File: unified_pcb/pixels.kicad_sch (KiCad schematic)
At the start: 291 parts

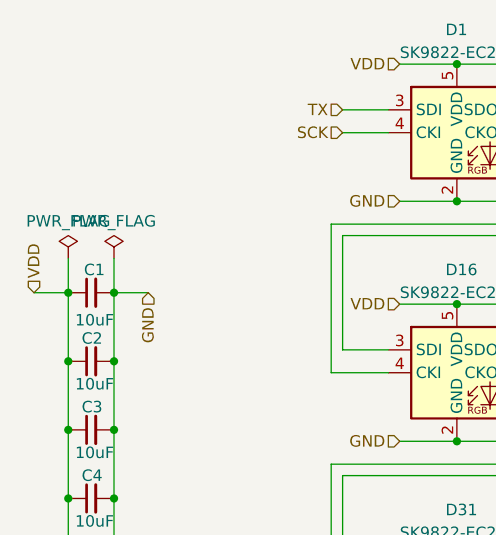
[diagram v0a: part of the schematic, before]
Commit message: change BQ27421 back to BQ27427
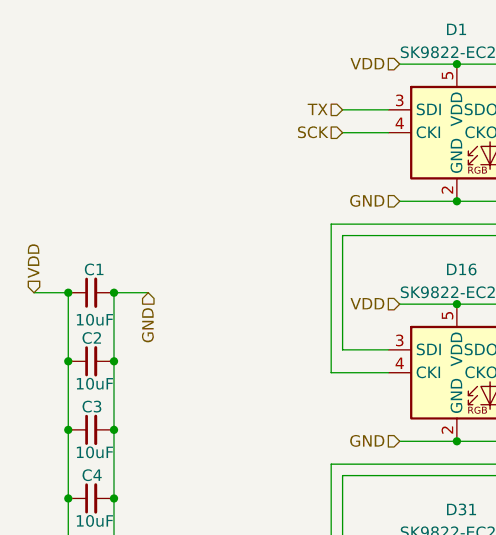
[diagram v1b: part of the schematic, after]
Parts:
- D1, D10, D100, D101, D102, D103, D104, D105, D106, D107, D108, D109, D11, D110, D111, D112, D113, D114, D115, D116, D117, D118, D119, D12, D120, D121, D122, D123, D124, D125, D126, D127, D128, D129, D13, D130, D131, D132, D133, D134, D135, D136, D137, D138, D139, D14, D140, D141, D142, D143, D144, D145, D146, D147, D148, D149, D15, D150, D151, D152, D153, D154, D155, D156, D157, D158, D159, D16, D160, D161, D162, D163, D164, D165, D166, D167, D168, D169, D17, D170, D171, D172, D173, D174, D175, D176, D177, D178, D179, D18, D180, D181, D182, D183, D184, D185, D186, D187, D188, D189, D19, D190, D191, D192, D193, D194, D195, D196, D197, D198, D199, D2, D20, D200, D201, D202, D203, D204, D205, D206, D207, D208, D209, D21, D210, D211, D212, D213, D214, D215, D216, D217, D218, D219, D22, D220, D221, D222, D223, D224, D225, D226, D227, D228, D229, D23, D230, D231, D232, D233, D234, D235, D236, D237, D238, D239, D24, D240, D241, D242, D243, D244, D245, D246, D247, D248, D249, D25, D250, D251, D252, D253, D254, D255, D256, D257, D258, D259, D26, D260, D261, D262, D263, D264, D265, D266, D267, D268, D269, D27, D270, D271, D28, D29, D3, D30, D31, D32, D33, D34, D35, D36, D37, D38, D39, D4, D40, D41, D42, D43, D44, D45, D46, D47, D48, D49, D5, D50, D51, D52, D53, D54, D55, D56, D57, D58, D59, D6, D60, D61, D62, D63, D64, D65, D66, D67, D68, D69, D7, D70, D71, D72, D73, D74, D75, D76, D77, D78, D79, D8, D80, D81, D82, D83, D84, D85, D86, D87, D88, D89, D9, D90, D91, D92, D93, D94, D95, D96, D97, D98, D99: Designation (none) -> SK9822-EC20; LCSC (none) -> C2909059

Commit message: part nums and bom rationalization
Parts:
- C1, C10, C11, C12, C13, C14, C15, C16, C17, C18, C19, C2, C20, C3, C4, C5, C6, C7, C8, C9: Designation (none) -> CL05A106MP5NUNC; LCSC (none) -> C315248
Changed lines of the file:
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@@
 			)
 		)
-		(property "Designation" ""
+		(property "LCSC" "C315248"
+			(at 57.15 90.17 0)
+			(effects
+				(font
+					(size 1.27 1.27)
+				)
+				(hide yes)
+			)
+		)
+		(property "Designation" "CL05A106MP5NUNC"
 			(at 57.15 90.17 0)
 			(effects
@@
 			)
 		)
-		(property "Designation" ""
+		(property "LCSC" "C315248"
+			(at 57.15 189.23 0)
+			(effects
+				(font
+					(size 1.27 1.27)
+				)
+				(hide yes)
+			)
+		)
+		(property "Designation" "CL05A106MP5NUNC"
 			(at 57.15 189.23 0)
 			(effects
@@
 			)
 		)
-		(property "Designation" ""
+		(property "LCSC" "C315248"
+			(at 57.15 82.55 0)
+			(effects
+				(font
+					(size 1.27 1.27)
+				)
+				(hide yes)
+			)
+		)
+		(property "Designation" "CL05A106MP5NUNC"
 			(at 57.15 82.55 0)
 			(effects
@@
 			)
 		)
-		(property "Designation" ""
+		(property "LCSC" "C315248"
+			(at 57.15 143.51 0)
+			(effects
+				(font
+					(size 1.27 1.27)
+				)
+				(hide yes)
+			)
+		)
+		(property "Designation" "CL05A106MP5NUNC"
 			(at 57.15 143.51 0)
 			(effects
@@
 			)
 		)
-		(property "Designation" ""
+		(property "LCSC" "C315248"
+			(at 57.15 173.99 0)
+			(effects
+				(font
+					(size 1.27 1.27)
+				)
+				(hide yes)
+			)
+		)
+		(property "Designation" "CL05A106MP5NUNC"
 			(at 57.15 173.99 0)
 			(effects
@@
 			)
 		)
-		(property "Designation" ""
+		(property "LCSC" "C315248"
+			(at 57.15 181.61 0)
+			(effects
+				(font
+					(size 1.27 1.27)
+				)
+				(hide yes)
+			)
+		)
+		(property "Designation" "CL05A106MP5NUNC"
 			(at 57.15 181.61 0)
 			(effects
@@
 			)
 		)
-		(property "Designation" ""
+		(property "LCSC" "C315248"
+			(at 57.15 151.13 0)
+			(effects
+				(font
+					(size 1.27 1.27)
+				)
+				(hide yes)
+			)
+		)
+		(property "Designation" "CL05A106MP5NUNC"
 			(at 57.15 151.13 0)
 			(effects
@@
 			)
 		)
-		(property "Designation" ""
+		(property "LCSC" "C315248"
+			(at 57.15 105.41 0)
+			(effects
+				(font
+					(size 1.27 1.27)
+				)
+				(hide yes)
+			)
+		)
+		(property "Designation" "CL05A106MP5NUNC"
 			(at 57.15 105.41 0)
 			(effects
@@
 			)
 		)
-		(property "Designation" ""
+		(property "LCSC" "C315248"
+			(at 57.15 74.93 0)
+			(effects
+				(font
+					(size 1.27 1.27)
+				)
+				(hide yes)
+			)
+		)
+		(property "Designation" "CL05A106MP5NUNC"
 			(at 57.15 74.93 0)
 			(effects
@@
 			)
 		)
-		(property "Designation" ""
+		(property "LCSC" "C315248"
+			(at 57.15 128.27 0)
+			(effects
+				(font
+					(size 1.27 1.27)
+				)
+				(hide yes)
+			)
+		)
+		(property "Designation" "CL05A106MP5NUNC"
 			(at 57.15 128.27 0)
 			(effects
@@
 			)
 		)
-		(property "Designation" ""
+		(property "LCSC" "C315248"
+			(at 57.15 120.65 0)
+			(effects
+				(font
+					(size 1.27 1.27)
+				)
+				(hide yes)
+			)
+		)
+		(property "Designation" "CL05A106MP5NUNC"
 			(at 57.15 120.65 0)
 			(effects
@@
 			)
 		)
-		(property "Designation" ""
+		(property "LCSC" "C315248"
+			(at 57.15 166.37 0)
+			(effects
+				(font
+					(size 1.27 1.27)
+				)
+				(hide yes)
+			)
+		)
+		(property "Designation" "CL05A106MP5NUNC"
 			(at 57.15 166.37 0)
 			(effects
@@
 			)
 		)
-		(property "Designation" ""
+		(property "LCSC" "C315248"
+			(at 57.15 196.85 0)
+			(effects
+				(font
+					(size 1.27 1.27)
+				)
+				(hide yes)
+			)
+		)
+		(property "Designation" "CL05A106MP5NUNC"
 			(at 57.15 196.85 0)
 			(effects
@@
 			)
 		)
-		(property "Designation" ""
+		(property "LCSC" "C315248"
+			(at 57.15 59.69 0)
+			(effects
+				(font
+					(size 1.27 1.27)
+				)
+				(hide yes)
+			)
+		)
+		(property "Designation" "CL05A106MP5NUNC"
 			(at 57.15 59.69 0)
 			(effects
@@
 			)
 		)
-		(property "Designation" ""
+		(property "LCSC" "C315248"
+			(at 57.15 158.75 0)
+			(effects
+				(font
+					(size 1.27 1.27)
+				)
+				(hide yes)
+			)
+		)
+		(property "Designation" "CL05A106MP5NUNC"
 			(at 57.15 158.75 0)
 			(effects
@@
 			)
 		)
-		(property "Designation" ""
+		(property "LCSC" "C315248"
+			(at 57.15 67.31 0)
+			(effects
+				(font
+					(size 1.27 1.27)
+				)
+				(hide yes)
+			)
+		)
+		(property "Designation" "CL05A106MP5NUNC"
 			(at 57.15 67.31 0)
 			(effects
@@
 			)
 		)
-		(property "Designation" ""
+		(property "LCSC" "C315248"
+			(at 57.15 113.03 0)
+			(effects
+				(font
+					(size 1.27 1.27)
+				)
+				(hide yes)
+			)
+		)
+		(property "Designation" "CL05A106MP5NUNC"
 			(at 57.15 113.03 0)
 			(effects
@@
 			)
 		)
-		(property "Designation" ""
+		(property "LCSC" "C315248"
+			(at 57.15 135.89 0)
+			(effects
+				(font
+					(size 1.27 1.27)
+				)
+				(hide yes)
+			)
+		)
+		(property "Designation" "CL05A106MP5NUNC"
 			(at 57.15 135.89 0)
 			(effects
@@
 			)
 		)
-		(property "Designation" ""
+		(property "LCSC" "C315248"
+			(at 57.15 97.79 0)
+			(effects
+				(font
+					(size 1.27 1.27)
+				)
+				(hide yes)
+			)
+		)
+		(property "Designation" "CL05A106MP5NUNC"
 			(at 57.15 97.79 0)
 			(effects
@@
 			)
 		)
-		(property "Designation" ""
+		(property "LCSC" "C315248"
+			(at 57.15 52.07 0)
+			(effects
+				(font
+					(size 1.27 1.27)
+				)
+				(hide yes)
+			)
+		)
+		(property "Designation" "CL05A106MP5NUNC"
 			(at 57.15 52.07 0)
 			(effects
